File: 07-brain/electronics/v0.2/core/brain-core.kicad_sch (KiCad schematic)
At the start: 12 parts, among them J1 Conn_02x03_Odd_Even, J10 Conn_01x02, J2 Conn_02x02_Odd_Even, J3 Conn_02x02_Odd_Even, J7 Conn_02x05_Odd_Even, J8 Conn_02x03_Odd_Even, J9 Conn_01x02

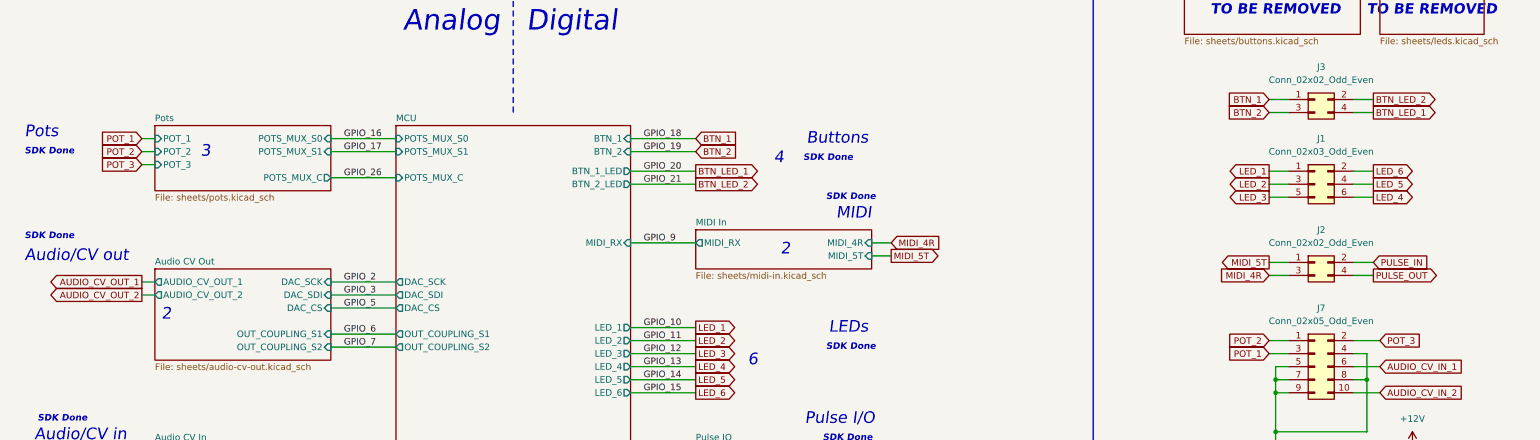
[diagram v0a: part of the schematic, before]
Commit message: Removed one pot and added one button in Brain
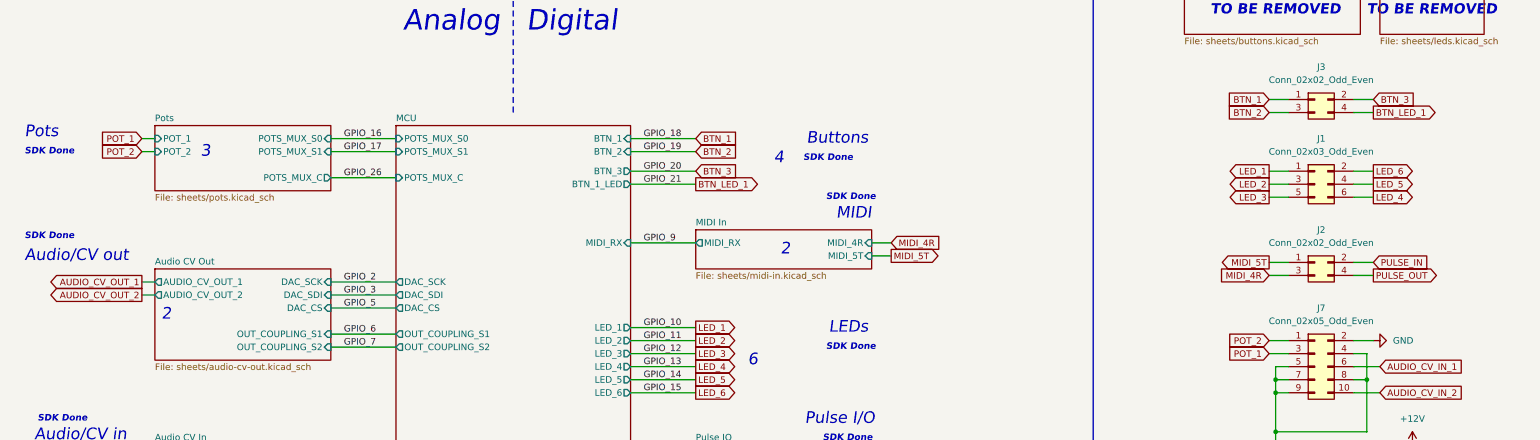
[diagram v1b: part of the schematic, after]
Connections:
- net POT_3 is gone; now on net GND: J7.2 (Pin_2)
- net BTN_LED_2 renamed BTN_3
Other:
- sheet MCU ports: added BTN_3; removed BTN_2_LED
- sheet Pots ports: added none; removed POT_3
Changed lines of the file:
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@@
 	(wire
 		(pts
-			(xy 52.07 58.42) (xy 54.61 58.42)
-		)
-		(stroke
-			(width 0)
-			(type default)
-		)
-	)
-	(wire
-		(pts
 			(xy 88.9 115.57) (xy 101.6 115.57)
 		)
@@
 	(wire
 		(pts
+			(xy 288.29 92.71) (xy 292.1 92.71)
+		)
+		(stroke
+			(width 0)
+			(type default)
+		)
+	)
+	(wire
+		(pts
 			(xy 52.07 115.57) (xy 54.61 115.57)
 		)
@@
 	(wire
 		(pts
-			(xy 288.29 92.71) (xy 293.37 92.71)
-		)
-		(stroke
-			(width 0)
-			(type default)
-		)
-	)
-	(wire
-		(pts
 			(xy 269.24 146.05) (xy 275.59 146.05)
 		)
@@
 		)
 	)
-	(global_label "POT_3"
-		(shape input)
-		(at 52.07 58.42 180)
-		(fields_autoplaced yes)
-		(effects
-			(font
-				(size 1.27 1.27)
-			)
-			(justify right)
-		)
-		(property "Intersheetrefs" "${INTERSHEET_REFS}"
-			(at 43.3396 58.42 0)
-			(effects
-				(font
-					(size 1.27 1.27)
-				)
-				(justify right)
-				(hide yes)
-			)
-		)
-	)
 	(global_label "AUDIO_CV_IN_2"
 		(shape input)
@@
 		)
 	)
-	(global_label "BTN_LED_2"
+	(global_label "BTN_LED_1"
 		(shape output)
 		(at 160.02 62.23 0)
@@
 		)
 	)
+	(global_label "BTN_3"
+		(shape input)
+		(at 160.02 59.69 0)
+		(fields_autoplaced yes)
+		(effects
+			(font
+				(size 1.27 1.27)
+			)
+			(justify left)
+		)
+		(property "Intersheetrefs" "${INTERSHEET_REFS}"
+			(at 168.7504 59.69 0)
+			(effects
+				(font
+					(size 1.27 1.27)
+				)
+				(justify left)
+				(hide yes)
+			)
+		)
+	)
 	(global_label "PULSE_IN"
 		(shape input)
@@
 		)
 	)
-	(global_label "BTN_LED_2"
-		(shape output)
+	(global_label "BTN_3"
+		(shape input)
 		(at 292.1 45.72 0)
 		(fields_autoplaced yes)
@@
 		)
 		(property "Intersheetrefs" "${INTERSHEET_REFS}"
-			(at 305.2451 45.72 0)
-			(effects
-				(font
-					(size 1.27 1.27)
-				)
-				(justify left)
-				(hide yes)
-			)
-		)
-	)
-	(global_label "BTN_LED_1"
-		(shape output)
-		(at 160.02 59.69 0)
-		(fields_autoplaced yes)
-		(effects
-			(font
-				(size 1.27 1.27)
-			)
-			(justify left)
-		)
-		(property "Intersheetrefs" "${INTERSHEET_REFS}"
-			(at 173.1651 59.69 0)
+			(at 300.8304 45.72 0)
 			(effects
 				(font
@@
 		)
 	)
-	(global_label "POT_3"
-		(shape input)
-		(at 293.37 92.71 0)
-		(fields_autoplaced yes)
-		(effects
-			(font
-				(size 1.27 1.27)
-			)
-			(justify left)
-		)
-		(property "Intersheetrefs" "${INTERSHEET_REFS}"
-			(at 302.1004 92.71 0)
-			(effects
-				(font
-					(size 1.27 1.27)
-				)
-				(justify left)
-				(hide yes)
-			)
-		)
-	)
 	(global_label "PULSE_IN"
 		(shape input)
@@
 	)
 	(symbol
+		(lib_id "power:GND")
+		(at 292.1 92.71 90)
+		(unit 1)
+		(exclude_from_sim no)
+		(in_bom yes)
+		(on_board yes)
+		(dnp no)
+		(fields_autoplaced yes)
+		(property "Reference" "#PWR076"
+			(at 298.45 92.71 0)
+			(effects
+				(font
+					(size 1.27 1.27)
+				)
+				(hide yes)
+			)
+		)
+		(property "Value" "GND"
+			(at 295.91 92.7099 90)
+			(effects
+				(font
+					(size 1.27 1.27)
+				)
+				(justify right)
+			)
+		)
+		(property "Footprint" ""
+			(at 292.1 92.71 0)
+			(effects
+				(font
+					(size 1.27 1.27)
+				)
+				(hide yes)
+			)
+		)
+		(property "Datasheet" ""
+			(at 292.1 92.71 0)
+			(effects
+				(font
+					(size 1.27 1.27)
+				)
+				(hide yes)
+			)
+		)
+		(property "Description" "Power symbol creates a global label with name \"GND\" , ground"
+			(at 292.1 92.71 0)
+			(effects
+				(font
+					(size 1.27 1.27)
+				)
+				(hide yes)
+			)
+		)
+		(pin "1"
+		)
+		(instances
+			(project ""
+				(path "/8e2e31f3-eed5-4de1-966c-f4162758c735"
+					(reference "#PWR076")
+					(unit 1)
+				)
+			)
+		)
+	)
+	(symbol
 		(lib_id "Mechanical:MountingHole")
 		(at 264.16 160.02 0)
@@
 			)
 		)
-		(pin "POT_3" input
-			(at 54.61 58.42 180)
-			(effects
-				(font
-					(size 1.27 1.27)
-				)
-				(justify left)
-			)
-		)
 		(instances
 			(project "brain-core"
@@
 			)
 		)
-		(pin "BTN_1_LED" output
+		(pin "BTN_3" output
 			(at 147.32 59.69 0)
 			(effects
@@
 			)
 		)
-		(pin "BTN_2_LED" output
+		(pin "BTN_1_LED" output
 			(at 147.32 62.23 0)
 			(effects

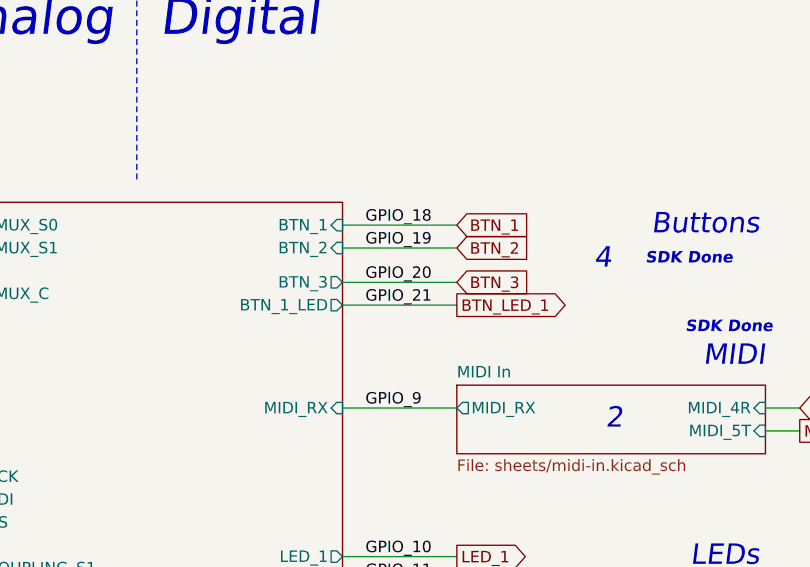
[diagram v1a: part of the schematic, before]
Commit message: Updated pull-up for MIDI opto in v0.2 Brain
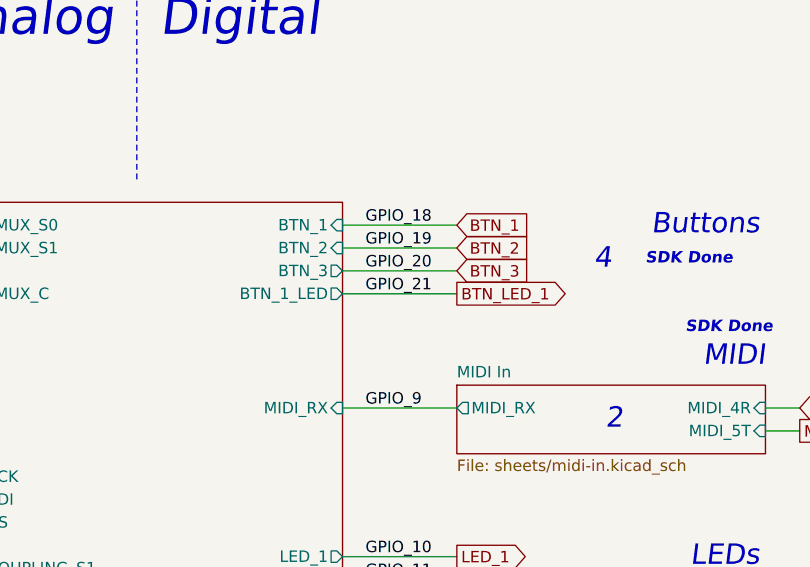
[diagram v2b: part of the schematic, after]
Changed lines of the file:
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@@
 	(wire
 		(pts
-			(xy 147.32 59.69) (xy 160.02 59.69)
+			(xy 147.32 58.42) (xy 160.02 58.42)
 		)
 		(stroke
@@
 	(wire
 		(pts
-			(xy 147.32 62.23) (xy 160.02 62.23)
+			(xy 147.32 60.96) (xy 160.02 60.96)
 		)
 		(stroke
@@
 	)
 	(label "GPIO_21"
-		(at 149.86 62.23 0)
+		(at 149.86 60.96 0)
 		(effects
 			(font
@@
 	)
 	(label "GPIO_20"
-		(at 149.86 59.69 0)
+		(at 149.86 58.42 0)
 		(effects
 			(font
@@
 	(global_label "BTN_LED_1"
 		(shape output)
-		(at 160.02 62.23 0)
+		(at 160.02 60.96 0)
 		(fields_autoplaced yes)
 		(effects
@@
 		)
 		(property "Intersheetrefs" "${INTERSHEET_REFS}"
-			(at 173.1651 62.23 0)
+			(at 173.1651 60.96 0)
 			(effects
 				(font
@@
 	(global_label "BTN_3"
 		(shape input)
-		(at 160.02 59.69 0)
+		(at 160.02 58.42 0)
 		(fields_autoplaced yes)
 		(effects
@@
 		)
 		(property "Intersheetrefs" "${INTERSHEET_REFS}"
-			(at 168.7504 59.69 0)
+			(at 168.7504 58.42 0)
 			(effects
 				(font
@@
 		)
 		(pin "BTN_3" output
-			(at 147.32 59.69 0)
+			(at 147.32 58.42 0)
 			(effects
 				(font
@@
 		)
 		(pin "BTN_1_LED" output
-			(at 147.32 62.23 0)
+			(at 147.32 60.96 0)
 			(effects
 				(font
